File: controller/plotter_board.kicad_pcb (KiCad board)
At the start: 2 copper layers, 100.1 x 100.1 mm, 89 parts, among them IC1 TMC2208, IC2 TMC2208, J1 Extenal_power, J10 PSU, J2 USB_Serial, J3 SD_Card, J4 OLED, J5 LEDS, J6 Stepper_ribbon, J7 Control_buttons, J8 Stepper_short, J9 Pen_Buttons, Q1 AO3400A, Q2 2N7002, Q3 2N7002, Q4 AO3401A, Q5 AO3401A, U1 ESP32-WROOM, U2 PCA9539PW, U3 AZ1117-3.3

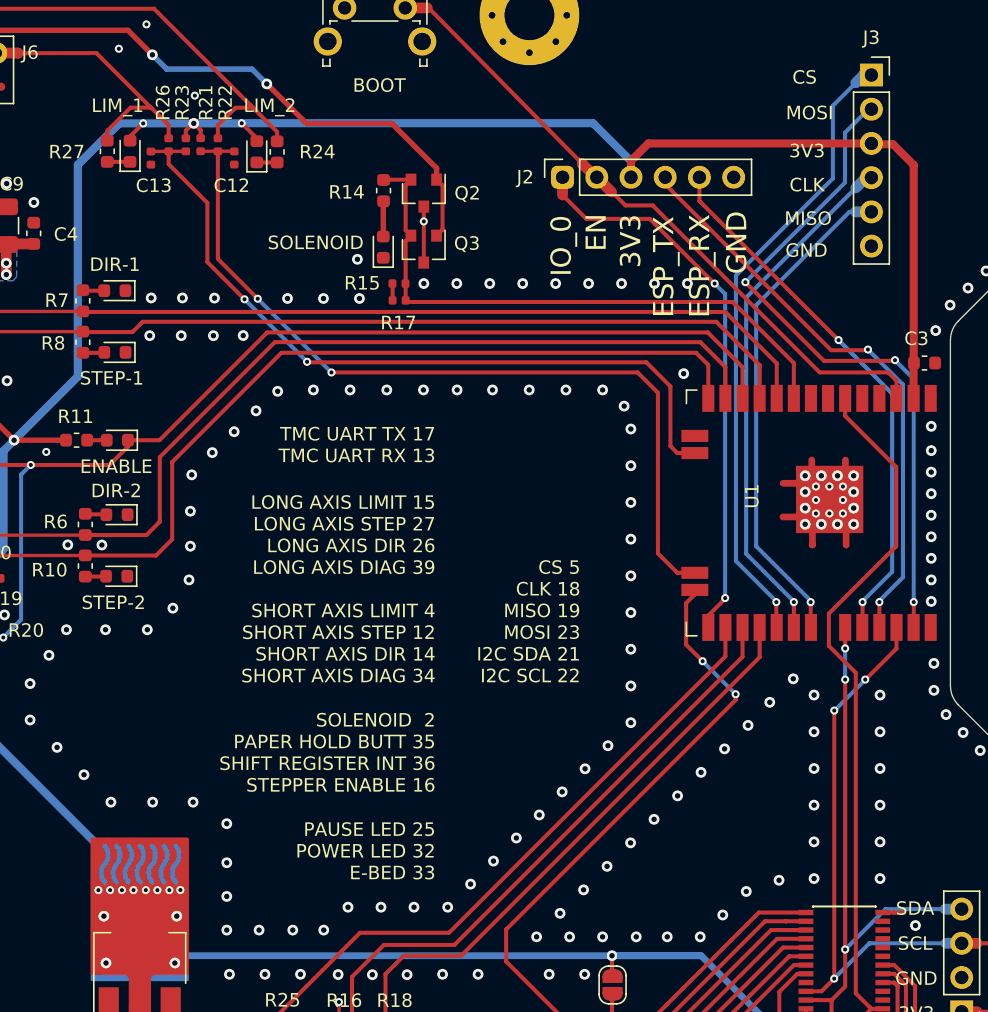
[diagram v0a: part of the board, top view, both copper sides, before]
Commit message: Fix pin maps
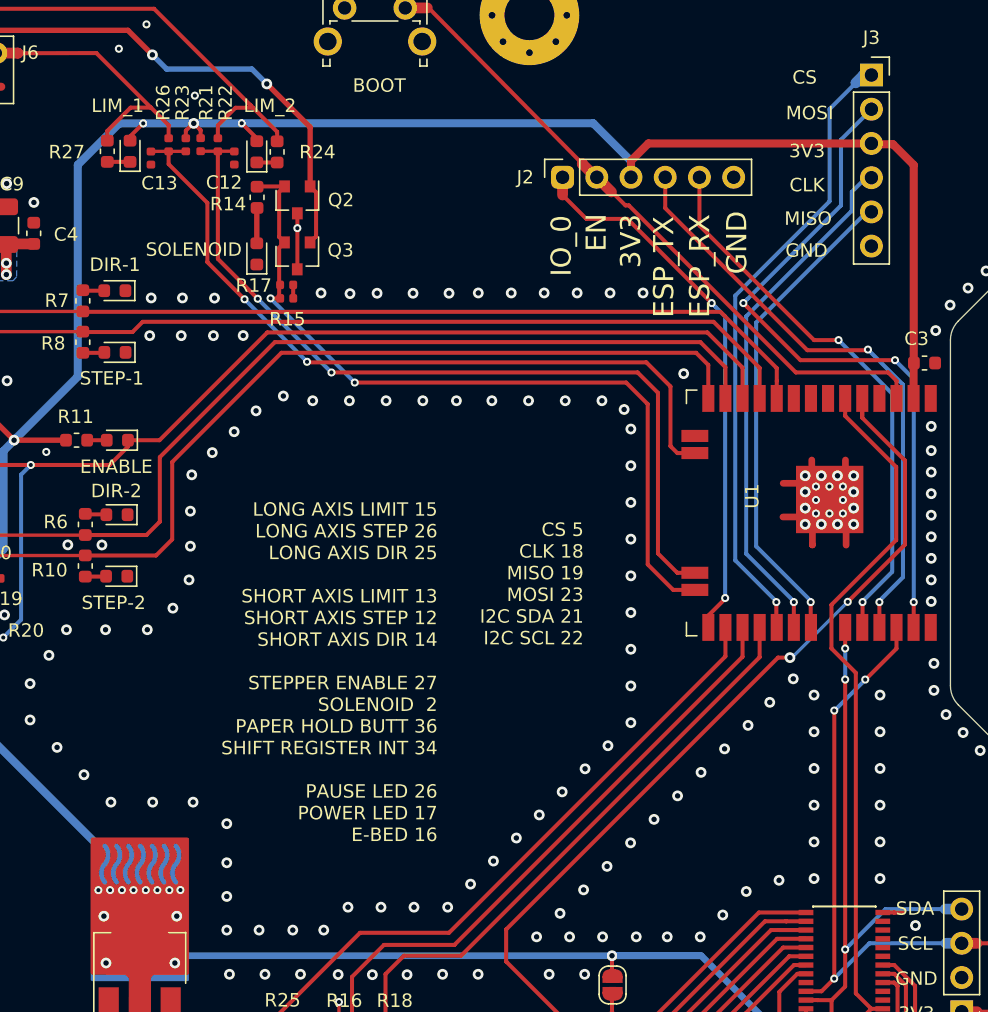
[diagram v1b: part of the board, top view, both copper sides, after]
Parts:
- moved Q2 9.40 mm to (143.5, 70.0)
- moved Q3 9.40 mm to (143.5, 74.1)
- moved D6 9.40 mm to (140.5, 74.0)
- moved R14 9.40 mm to (140.6, 69.8)
- moved R17 8.43 mm to (142.7, 76.3), turned to 0 degrees
- moved R15 8.41 mm to (142.8, 77.3), turned to 0 degrees
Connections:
- IC1 pad 29: GND -> (no net)
- IC2 pad 29: GND -> (no net)
- U1 pad 24: PAPER_HOLD -> PWM_SOLENOID
- U1 pad 5: Net-(U1-Pad5) -> PAPER_HOLD
- U1 pad 9: PWM_SOLENOID -> Net-(U1-Pad9)
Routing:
- net PAPER_HOLD: track 88.3 -> 108.9 mm
- net PWM_SOLENOID: track 45.0 -> 59.4 mm, vias 0 -> 2
- net SOLENOID_O: track 57.3 -> 50.2 mm
- net CLK: track 40.0 -> 38.9 mm
- net TX: track 40.2 -> 41.3 mm
- net RX: track 43.1 -> 44.1 mm
- net IO_0: track 42.9 -> 41.9 mm
- net MOSI: track 50.8 -> 51.7 mm
- net MISO: track 37.0 -> 36.3 mm
- net GND: track 39.4 -> 39.0 mm, vias 443 -> 441
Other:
- board text added: "LONG AXIS LIMIT 15 LONG AXIS STEP 26 LONG AXIS DIR 25 SHORT AXIS LIMIT 13 SHORT AXIS STEP 12 SHORT AXIS DIR 14 STEPPER ENABLE 27 SOLENOID 2 PAPER HOLD BUTT 36 SHIFT REGISTER INT 34 PAUSE LED 26 POWER LED 17 E-BED 16"
- board text removed: "LONG AXIS LIMIT 15 LONG AXIS STEP 27 LONG AXIS DIR 26 LONG AXIS DIAG 39 SHORT AXIS LIMIT 4 SHORT AXIS STEP 12 SHORT AXIS DIR 14 SHORT AXIS DIAG 34"
- board text removed: "PAUSE LED 25 POWER LED 32 E-BED 33"
- board text removed: "SOLENOID 2 PAPER HOLD BUTT 35 SHIFT REGISTER INT 36 STEPPER ENABLE 16"
- board text removed: "TMC UART TX 17 TMC UART RX 13"

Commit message: Upload files
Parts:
- removed the R20 at (120.5, 102.0)
- removed R29: 0R56, Resistor_SMD:R_1206_3216Metric
- removed the R3 at (117.9, 82.5)
- removed the R5 at (115.3, 83.4)
- removed REF** (x3): MountingHole_3.7mm_Pad_Via, MountingHole:MountingHole_3.7mm_Pad_Via
- added H5: MountingHole, MountingHole:MountingHole_3.7mm_Pad_Via, F.Cu at (102.0, 56.3)
- added H6: MountingHole, MountingHole:MountingHole_3.7mm_Pad_Via, F.Cu at (160.8, 56.3)
- added H7: MountingHole, MountingHole:MountingHole_3.7mm_Pad_Via, F.Cu at (102.0, 148.6)
- added R27: 0R56, Resistor_SMD:R_1206_3216Metric, F.Cu at (109.0, 102.2)
- added R4: 22k, Resistor_SMD:R_0402_1005Metric, F.Cu at (115.3, 82.6)
- added R9: 4K7, Resistor_SMD:R_0402_1005Metric, F.Cu at (170.2, 90.3)
- IC1, IC2: value TMC2208 -> TMC2209
- J10: footprint Connector_Molex:Molex_SPOX_5267-09A_1x09_P2.50mm_Vertical -> plotter_board:Molex_SPOX_5267-09A_1x09_P2.50mm_Vertical
- J5: footprint Connector_Molex:Molex_SPOX_5267-06A_1x06_P2.50mm_Vertical -> plotter_board:Molex_SPOX_5267-06A_1x06_P2.50mm_Vertical
- J7: footprint Connector_Molex:Molex_SPOX_5267-10A_1x10_P2.50mm_Vertical -> plotter_board:Molex_SPOX_5267-10A_1x10_P2.50mm_Vertical
- J9: footprint Connector_Molex:Molex_SPOX_5267-12A_1x12_P2.50mm_Vertical -> plotter_board:Molex_SPOX_5267-12A_1x12_P2.50mm_Vertical
- R19: value 10K -> 22k
- moved C10 4.61 mm to (119.5, 102.4), turned to 90 degrees
- moved R28 3.61 mm to (109.0, 98.6)
- moved R15 3.21 mm to (140.8, 74.8), turned to 180 degrees
- moved R19 3.09 mm to (120.5, 102.4), turned to 270 degrees
- moved R17 2.07 mm to (140.8, 75.7)
- moved D6 1.21 mm to (140.6, 72.8)
- moved J8 0.94 mm to (101.9, 97.4)
- moved C1 0.74 mm to (119.8, 82.7)
- moved C14 0.25 mm to (109.8, 107.3)
- moved C18 0.16 mm to (109.0, 105.4)
- moved C7 0.14 mm to (109.7, 72.5)
- moved C11 0.12 mm to (118.3, 104.6)
- moved C19 0.11 mm to (109.0, 95.5)
- moved IC2 0.10 mm to (115.9, 100.4)
- moved C15 0.10 mm to (117.0, 104.6)
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- renumbered D3 to D2, D2 to D3, D5 to D4, D4 to D5, R21 to R20, R22 to R21, R23 to R22, R24 to R23, R25 to R24, R26 to R25, R27 to R26, R4 to R3, R8 to R5, R7 to R6, R6 to R7, R9 to R8
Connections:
- IC1 pad 11: Net-(IC1-Pad11) -> SHORT_DIAG
- IC1 pad 14: Net-(IC1-Pad14) -> TMC_UART
- IC1 pad 29: (no net) -> GND
- IC2 pad 10: +3V3 -> GND
- IC2 pad 11: Net-(IC2-Pad11) -> LONG_DIAG
- IC2 pad 14: Net-(IC2-Pad14) -> TMC_UART
- IC2 pad 29: (no net) -> GND
- R19 pad 1: GND -> +3V3
- R19 pad 2: Net-(IC2-Pad14) -> STEP_EN
- R28 pad 2: Net-(IC2-Pad27) -> Net-(IC2-Pad23)
- U1 pad 16: SHORT_AXIS_LIMIT_O -> SHORT_DIAG
- U1 pad 23: LONG_AXIS_LIMIT_O -> LONG_DIAG
- U1 pad 4: Net-(U1-Pad4) -> LONG_AXIS_LIMIT_O
- U1 pad 7: Net-(U1-Pad7) -> SHORT_AXIS_LIMIT_O
- U1 pad 8: Net-(U1-Pad8) -> TMC_UART_RX
- U1 pad 9: Net-(U1-Pad9) -> TMC_UART
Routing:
- net TMC_UART: track 0.00 -> 96.6 mm, vias 0 -> 5
- net LONG_DIAG: track 0.00 -> 75.4 mm, vias 0 -> 2
- net SHORT_DIAG: track 0.00 -> 62.4 mm, vias 0 -> 4
- net TMC_UART_RX: track 0.00 -> 15.0 mm
- net SHORT_AXIS_LIMIT_O: track 56.6 -> 63.8 mm, vias 2 -> 0
- net 36V: track 41.0 -> 45.2 mm, vias 20 -> 22
- net STEP_EN: track 102.3 -> 106.2 mm, vias 6 -> 5
- net +3V3: track 264.0 -> 261.1 mm, vias 19 -> 21
- net LONG_AXIS_LIMIT_O: track 62.6 -> 65.4 mm, vias 2 -> 0
- net STEP_LONG_RED: track 11.1 -> 13.0 mm
- net MOSI: track 51.7 -> 49.8 mm
- net Net-(IC2-Pad14): track 1.31 -> 0.00 mm
- net Net-(IC1-Pad14): track 1.31 -> 0.00 mm
- net STEP_LONG_YELLOW: track 11.9 -> 13.2 mm
- net Net-(D6-Pad2): track 2.56 -> 1.39 mm
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- added copper zone on B.Cu, net Net-(J10-Pad3)
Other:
- board text added: "LONG AXIS LIMIT 36 LONG AXIS STEP 26 LONG AXIS DIR 25 lONG AXIS DIAG 15 SHORT AXIS LIMIT 35 SHORT AXIS STEP 12 SHORT AXIS DIR 14 SHORT AXIS DIAG 13 TMC UART TX 33 TMC UART RX 32 STEPPER ENABLE 27 SOLENOID 2 PAPER HOLD BUTT 39 SHIFT REGISTER INT 34 PAUSE LED 4 POWER LED 17 E-BED 16"
- board text removed: "LONG AXIS LIMIT 15 LONG AXIS STEP 26 LONG AXIS DIR 25 SHORT AXIS LIMIT 13 SHORT AXIS STEP 12 SHORT AXIS DIR 14 STEPPER ENABLE 27 SOLENOID 2 PAPER HOLD BUTT 36 SHIFT REGISTER INT 34 PAUSE LED 26 POWER LED 17 E-BED 16"
